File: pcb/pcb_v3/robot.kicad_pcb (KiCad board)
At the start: 2 copper layers, 34.9 x 82.5 mm, 34 parts, among them J1 M1 PWR, J11 MB CTRL, J12 MA CTRL, J2 M2 PWR, J3 Power Connector, J4 BATT, J5 TB6612_Motor_Driver, J7 SWITCH, Q1 2N3904, Q2 2N3904, Q3 2N3906, U1 L7805, U3 L78L33

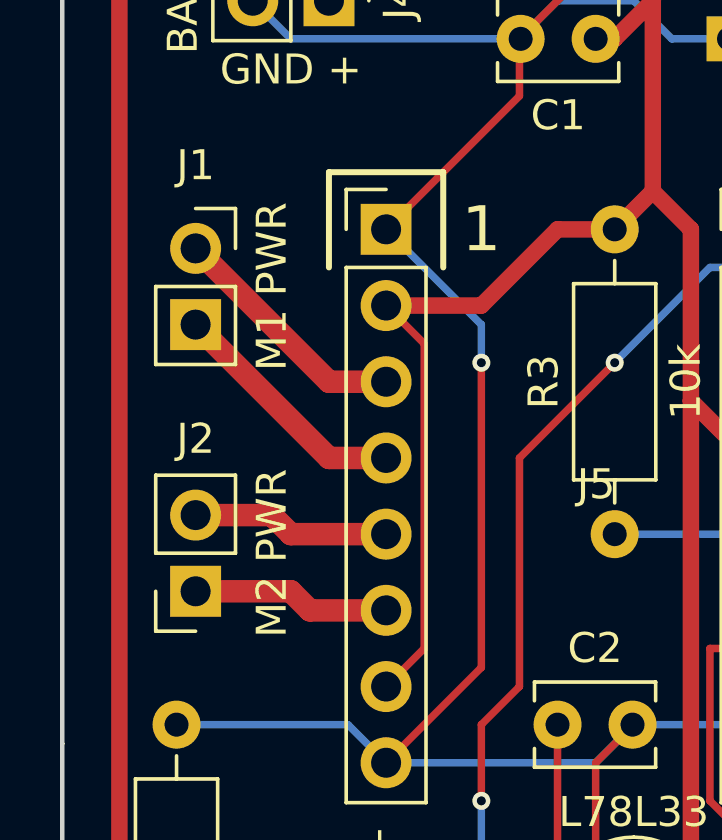
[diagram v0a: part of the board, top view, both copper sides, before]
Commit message: SMB, 28 Apr 2020, fixed error in PCB.
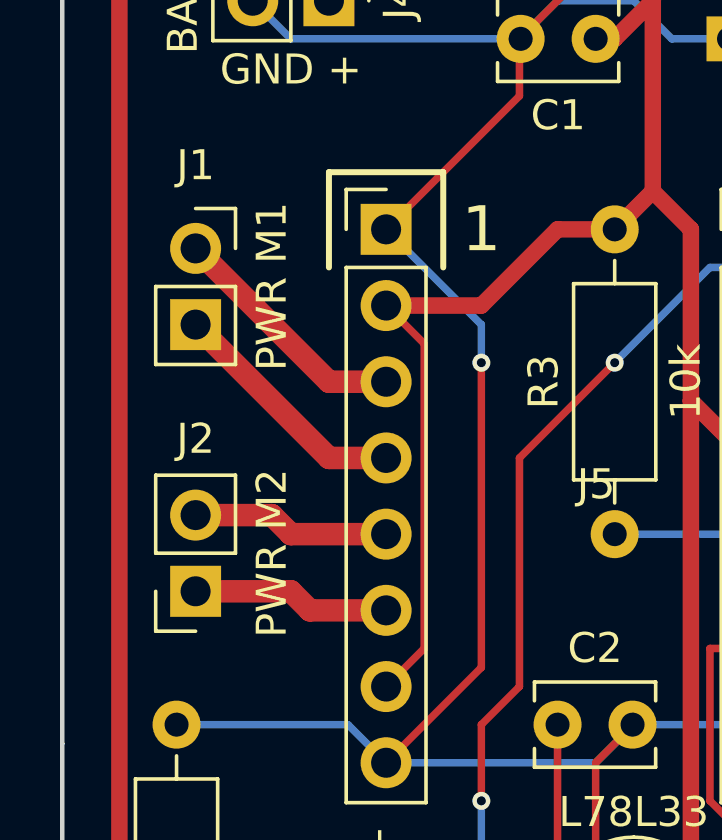
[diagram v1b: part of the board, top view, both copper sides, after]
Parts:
- J1: value M1 PWR -> PWR M1
- J2: value M2 PWR -> PWR M2
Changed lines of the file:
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@@
     (pcbplotparams
       (layerselection 0x010f0_ffffffff)
-      (usegerberextensions false)
+      (usegerberextensions true)
       (usegerberattributes false)
       (usegerberadvancedattributes false)
@@
       (effects (font (size 1 1) (thickness 0.15)))
     )
-    (fp_text value "M2 PWR" (at -2.54 1.27 270) (layer F.SilkS)
+    (fp_text value "PWR M2" (at -2.54 1.27 270) (layer F.SilkS)
       (effects (font (size 1 1) (thickness 0.15)))
     )
@@
       (effects (font (size 1 1) (thickness 0.15)))
     )
-    (fp_text value "M1 PWR" (at 2.54 1.27 90) (layer F.SilkS)
-      (effects (font (size 1 1) (thickness 0.15)))
-    )
+    (fp_text value "PWR M1" (at 2.54 1.27 90) (layer F.SilkS)
+      (effects (font (size 1 1) (thickness 0.15)))
+    )

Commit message: Same
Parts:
- J5: renamed from J1; value PWR M1 -> M1 PWR
- J6: renamed from J2; value PWR M2 -> M2 PWR
- renumbered J7 to J1, J4 to J2, J12 to J3, J11 to J4, J3 to J7, J5 to J8, U3 to U2
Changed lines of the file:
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@@
     (pcbplotparams
       (layerselection 0x010f0_ffffffff)
-      (usegerberextensions true)
+      (usegerberextensions false)
       (usegerberattributes false)
       (usegerberadvancedattributes false)
@@
   (net 12 "Net-(Q2-Pad2)")
   (net 13 +BATT)
-  (net 14 "Net-(J1-Pad1)")
-  (net 15 "Net-(J1-Pad2)")
-  (net 16 "Net-(J2-Pad1)")
-  (net 17 "Net-(J2-Pad2)")
-  (net 18 "Net-(J4-Pad1)")
+  (net 14 "Net-(J1-Pad2)")
+  (net 15 "Net-(J5-Pad2)")
+  (net 16 "Net-(J5-Pad1)")
+  (net 17 "Net-(J6-Pad2)")
+  (net 18 "Net-(J6-Pad1)")
   (net_class Default "This is the default net class."
     (clearance 0.2)
@@
     (add_net GND)
     (add_net "Net-(D1-Pad1)")
-    (add_net "Net-(J1-Pad1)")
+    (add_net "Net-(D2-Pad2)")
     (add_net "Net-(J1-Pad2)")
-    (add_net "Net-(J2-Pad1)")
-    (add_net "Net-(J2-Pad2)")
-    (add_net "Net-(J4-Pad1)")
+    (add_net "Net-(J5-Pad1)")
+    (add_net "Net-(J5-Pad2)")
+    (add_net "Net-(J6-Pad1)")
+    (add_net "Net-(J6-Pad2)")
     (add_net "Net-(Q1-Pad2)")
     (add_net "Net-(Q2-Pad2)")
+    (add_net "Net-(Q3-Pad2)")
+    (add_net "Net-(Q3-Pad3)")
+    (add_net "Net-(R2-Pad1)")
+    (add_net "Net-(R2-Pad2)")
+    (add_net "Net-(R7-Pad1)")
+    (add_net "Net-(R7-Pad2)")
+    (add_net "Net-(R8-Pad1)")
+    (add_net "Net-(R8-Pad2)")
   )
   (net_class power ""
@@
     (descr "Through hole motor driver")
     (tags "Motor driver")
-    (fp_text reference J5 (at 7 8.5) (layer F.SilkS)
+    (fp_text reference J8 (at 7 8.5) (layer F.SilkS)
       (effects (font (size 1 1) (thickness 0.15)))
     )
@@
       (net 2 +5V))
     (pad 6 thru_hole oval (at 0 12.7) (size 1.7 1.7) (drill 1) (layers *.Cu *.Mask)
-      (net 16 "Net-(J2-Pad1)"))
+      (net 18 "Net-(J6-Pad1)"))
     (pad 5 thru_hole oval (at 0 10.16) (size 1.7 1.7) (drill 1) (layers *.Cu *.Mask)
-      (net 17 "Net-(J2-Pad2)"))
+      (net 17 "Net-(J6-Pad2)"))
     (pad 4 thru_hole oval (at 0 7.62) (size 1.7 1.7) (drill 1) (layers *.Cu *.Mask)
-      (net 15 "Net-(J1-Pad2)"))
+      (net 15 "Net-(J5-Pad2)"))
     (pad 3 thru_hole oval (at 0 5.08) (size 1.7 1.7) (drill 1) (layers *.Cu *.Mask)
-      (net 14 "Net-(J1-Pad1)"))
+      (net 16 "Net-(J5-Pad1)"))
     (pad 2 thru_hole oval (at 0 2.54) (size 1.7 1.7) (drill 1) (layers *.Cu *.Mask)
       (net 2 +5V))
@@
     (descr "Through hole straight pin header, 1x02, 2.54mm pitch, single row")
     (tags "Through hole pin header THT 1x02 2.54mm single row")
-    (fp_text reference J4 (at 0 -2.33 90) (layer F.SilkS)
+    (fp_text reference J2 (at 0 -2.33 90) (layer F.SilkS)
       (effects (font (size 1 1) (thickness 0.15)))
     )
@@
       (net 1 GND))
     (pad 1 thru_hole rect (at 0 0 270) (size 1.7 1.7) (drill 1) (layers *.Cu *.Mask)
-      (net 18 "Net-(J4-Pad1)"))
+      (net 14 "Net-(J1-Pad2)"))
     (model ${KISYS3DMOD}/Connector_PinHeader_2.54mm.3dshapes/PinHeader_1x02_P2.54mm_Vertical.wrl
       (at (xyz 0 0 0))
@@
     (descr "Through hole straight pin header, 1x02, 2.54mm pitch, single row")
     (tags "Through hole pin header THT 1x02 2.54mm single row")
-    (fp_text reference J7 (at 0 -2.33 90) (layer F.SilkS)
+    (fp_text reference J1 (at 0 -2.33 90) (layer F.SilkS)
       (effects (font (size 1 1) (thickness 0.15)))
     )
@@
     (fp_line (start -0.635 -1.27) (end 1.27 -1.27) (layer F.Fab) (width 0.1))
     (pad 2 thru_hole rect (at 0 2.54 90) (size 1.7 1.7) (drill 1) (layers *.Cu *.Mask)
-      (net 18 "Net-(J4-Pad1)"))
+      (net 14 "Net-(J1-Pad2)"))
     (pad 1 thru_hole oval (at 0 0 90) (size 1.7 1.7) (drill 1) (layers *.Cu *.Mask)
       (net 13 +BATT))
@@
     (descr "Through hole straight socket strip, 2x05, 2.54mm pitch, double cols (from Kicad 4.0.7), script generated")
     (tags "Through hole socket strip THT 2x05 2.54mm double row")
-    (fp_text reference J3 (at -1.27 -2.77 90) (layer F.SilkS) hide
+    (fp_text reference J7 (at -1.27 -2.77 90) (layer F.SilkS) hide
       (effects (font (size 1 1) (thickness 0.15)))
     )
@@
     (descr "Through hole straight pin header, 1x02, 2.54mm pitch, single row")
     (tags "Through hole pin header THT 1x02 2.54mm single row")
-    (fp_text reference J12 (at 0 -2.33) (layer F.Fab)
+    (fp_text reference J3 (at 0.635 4.75) (layer F.SilkS)
       (effects (font (size 1 1) (thickness 0.15)))
     )
@@
     (descr "Through hole straight pin header, 1x02, 2.54mm pitch, single row")
     (tags "Through hole pin header THT 1x02 2.54mm single row")
-    (fp_text reference J11 (at 0 -2.33) (layer F.Fab)
+    (fp_text reference J4 (at -0.635 4.75) (layer F.SilkS)
       (effects (font (size 1 1) (thickness 0.15)))
     )
@@
     (descr "Through hole straight socket strip, 1x02, 2.54mm pitch, single row (from Kicad 4.0.7), script generated")
     (tags "Through hole socket strip THT 1x02 2.54mm single row")
-    (fp_text reference J2 (at 0 5.08) (layer F.SilkS)
-      (effects (font (size 1 1) (thickness 0.15)))
-    )
-    (fp_text value "PWR M2" (at -2.54 1.27 270) (layer F.SilkS)
+    (fp_text reference J6 (at 0 5.08) (layer F.SilkS)
+      (effects (font (size 1 1) (thickness 0.15)))
+    )
+    (fp_text value "M2 PWR" (at -2.54 1.27 270) (layer F.SilkS)
       (effects (font (size 1 1) (thickness 0.15)))
     )
@@
     (fp_line (start -1.27 -1.27) (end 0.635 -1.27) (layer F.Fab) (width 0.1))
     (pad 2 thru_hole oval (at 0 2.54 180) (size 1.7 1.7) (drill 1) (layers *.Cu *.Mask)
-      (net 17 "Net-(J2-Pad2)"))
+      (net 17 "Net-(J6-Pad2)"))
     (pad 1 thru_hole rect (at 0 0 180) (size 1.7 1.7) (drill 1) (layers *.Cu *.Mask)
-      (net 16 "Net-(J2-Pad1)"))
+      (net 18 "Net-(J6-Pad1)"))
     (model ${KISYS3DMOD}/Connector_PinSocket_2.54mm.3dshapes/PinSocket_1x02_P2.54mm_Vertical.wrl
       (at (xyz 0 0 0))
@@
     (descr "Through hole straight socket strip, 1x02, 2.54mm pitch, single row (from Kicad 4.0.7), script generated")
     (tags "Through hole socket strip THT 1x02 2.54mm single row")
-    (fp_text reference J1 (at 0 -2.77) (layer F.SilkS)
-      (effects (font (size 1 1) (thickness 0.15)))
-    )
-    (fp_text value "PWR M1" (at 2.54 1.27 90) (layer F.SilkS)
+    (fp_text reference J5 (at 0 -2.77) (layer F.SilkS)
+      (effects (font (size 1 1) (thickness 0.15)))
+    )
+    (fp_text value "M1 PWR" (at 2.54 1.27 90) (layer F.SilkS)
       (effects (font (size 1 1) (thickness 0.15)))
     )
@@
     (fp_line (start -1.27 -1.27) (end 0.635 -1.27) (layer F.Fab) (width 0.1))
     (pad 2 thru_hole rect (at 0 2.54) (size 1.7 1.7) (drill 1) (layers *.Cu *.Mask)
-      (net 15 "Net-(J1-Pad2)"))
+      (net 15 "Net-(J5-Pad2)"))
     (pad 1 thru_hole oval (at 0 0) (size 1.7 1.7) (drill 1) (layers *.Cu *.Mask)
-      (net 14 "Net-(J1-Pad1)"))
+      (net 16 "Net-(J5-Pad1)"))
     (model ${KISYS3DMOD}/Connector_PinSocket_2.54mm.3dshapes/PinSocket_1x02_P2.54mm_Vertical.wrl
       (at (xyz 0 0 0))
@@
     (fp_line (start 0.8 1.75) (end 4.3 1.75) (layer F.Fab) (width 0.1))
     (fp_line (start 0.74 1.85) (end 4.34 1.85) (layer F.SilkS) (width 0.12))
-    (fp_text user %R (at -2.54 -1.27) (layer F.Fab)
+    (fp_text user %R (at -2.54 -1.27) (layer F.Fab) hide
       (effects (font (size 1 1) (thickness 0.15)))
     )
@@
     (descr "TO-92L leads in-line (large body variant of TO-92), also known as TO-226, wide, drill 0.75mm (see https://www.diodes.com/assets/Package-Files/TO92L.pdf and http://www.ti.com/lit/an/snoa059/snoa059.pdf)")
     (tags "TO-92L Inline Wide transistor")
-    (fp_text reference U3 (at 2.54 -3.56) (layer F.Fab)
+    (fp_text reference U2 (at 2.54 -3.56) (layer F.Fab)
       (effects (font (size 1 1) (thickness 0.15)))
     )
@@
   (segment (start 102.87 35.56) (end 102.235 36.195) (width 0.55) (layer B.Cu) (net 13))
   (segment (start 102.87 27.94) (end 102.87 35.56) (width 0.55) (layer B.Cu) (net 13))
-  (segment (start 106.68 65.405) (end 104.775 65.405) (width 0.75) (layer F.Cu) (net 14))
-  (segment (start 104.775 65.405) (end 100.33 60.96) (width 0.75) (layer F.Cu) (net 14))
+  (segment (start 106.68 65.405) (end 104.775 65.405) (width 0.75) (layer F.Cu) (net 16))
+  (segment (start 104.775 65.405) (end 100.33 60.96) (width 0.75) (layer F.Cu) (net 16))
   (segment (start 106.68 67.945) (end 104.775 67.945) (width 0.75) (layer F.Cu) (net 15))
   (segment (start 104.775 67.945) (end 100.33 63.5) (width 0.75) (layer F.Cu) (net 15))
-  (segment (start 106.68 73.025) (end 104.14 73.025) (width 0.75) (layer F.Cu) (net 16))
-  (segment (start 103.505 72.39) (end 100.33 72.39) (width 0.75) (layer F.Cu) (net 16))
-  (segment (start 104.14 73.025) (end 103.505 72.39) (width 0.75) (layer F.Cu) (net 16))
+  (segment (start 106.68 73.025) (end 104.14 73.025) (width 0.75) (layer F.Cu) (net 18))
+  (segment (start 103.505 72.39) (end 100.33 72.39) (width 0.75) (layer F.Cu) (net 18))
+  (segment (start 104.14 73.025) (end 103.505 72.39) (width 0.75) (layer F.Cu) (net 18))
   (segment (start 106.68 70.485) (end 103.505 70.485) (width 0.75) (layer F.Cu) (net 17))
   (segment (start 102.87 69.85) (end 100.33 69.85) (width 0.75) (layer F.Cu) (net 17))
   (segment (start 103.505 70.485) (end 102.87 69.85) (width 0.75) (layer F.Cu) (net 17))
-  (segment (start 104.775 52.705) (end 104.775 46.99) (width 0.25) (layer B.Cu) (net 18) (status 80000))
+  (segment (start 104.775 52.705) (end 104.775 46.99) (width 0.25) (layer B.Cu) (net 14) (status 80000))
   (zone (net 1) (net_name GND) (layer F.Cu) (hatch edge 0.508)
     (connect_pads (clearance 0.508))
